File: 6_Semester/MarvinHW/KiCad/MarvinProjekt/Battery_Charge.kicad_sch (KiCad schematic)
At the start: 13 parts, among them U5 DW01A, U6 FS8205A, U7 HM4056H

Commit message: add comonents to BoM
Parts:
- BT1: OrderNow (none) -> x; digikey (none) -> 36-1043P-ND
- U5: LCSC Part (none) -> C351410; OrderNow (none) -> x
- U6: LCSC Part (none) -> C7499846; OrderNow (none) -> x
- U7: OrderNow (none) -> x
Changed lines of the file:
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@@
+			)
+		)
+		(property "OrderNow" ""
+			(at 156.21 95.25 0)
+			(effects
+				(font
+					(size 1.27 1.27)
+				)
+				(hide yes)
 			)
 		)
@@
 			)
 		)
+		(property "OrderNow" ""
+			(at 105.41 92.71 0)
+			(effects
+				(font
+					(size 1.27 1.27)
+				)
+				(hide yes)
+			)
+		)
 		(pin "2"
 		)
@@
 			)
 		)
+		(property "OrderNow" ""
+			(at 105.41 82.55 0)
+			(effects
+				(font
+					(size 1.27 1.27)
+				)
+				(hide yes)
+			)
+		)
 		(pin "1"
 		)
@@
 		)
 		(property "Description" "Resistor"
+			(at 191.77 106.68 0)
+			(effects
+				(font
+					(size 1.27 1.27)
+				)
+				(hide yes)
+			)
+		)
+		(property "OrderNow" ""
 			(at 191.77 106.68 0)
 			(effects
@@
 			)
 		)
+		(property "OrderNow" "x"
+			(at 119.38 92.71 0)
+			(effects
+				(font
+					(size 1.27 1.27)
+				)
+				(hide yes)
+			)
+		)
+		(property "LCSC Part" "C351410"
+			(at 119.38 92.71 0)
+			(effects
+				(font
+					(size 1.27 1.27)
+				)
+				(hide yes)
+			)
+		)
 		(pin "6"
 		)
@@
 			)
 		)
+		(property "OrderNow" "x"
+			(at 179.07 96.52 0)
+			(effects
+				(font
+					(size 1.27 1.27)
+				)
+				(hide yes)
+			)
+		)
 		(pin "3"
 		)
@@
 		)
 		(property "Description" "Unpolarized capacitor"
+			(at 143.51 99.06 0)
+			(effects
+				(font
+					(size 1.27 1.27)
+				)
+				(hide yes)
+			)
+		)
+		(property "OrderNow" ""
 			(at 143.51 99.06 0)
 			(effects
@@
 			)
 		)
+		(property "OrderNow" ""
+			(at 135.89 95.25 0)
+			(effects
+				(font
+					(size 1.27 1.27)
+				)
+				(hide yes)
+			)
+		)
 		(pin "1"
 		)
@@
 			)
 		)
+		(property "OrderNow" ""
+			(at 162.56 99.06 0)
+			(effects
+				(font
+					(size 1.27 1.27)
+				)
+				(hide yes)
+			)
+		)
 		(pin "1"
 		)
@@
 			)
 		)
+		(property "OrderNow" ""
+			(at 156.21 102.87 0)
+			(effects
+				(font
+					(size 1.27 1.27)
+				)
+				(hide yes)
+			)
+		)
 		(pin "1"
 		)
@@
 			)
 		)
+		(property "OrderNow" "x"
+			(at 97.79 88.9 0)
+			(effects
+				(font
+					(size 1.27 1.27)
+				)
+				(hide yes)
+			)
+		)
+		(property "digikey" "36-1043P-ND"
+			(at 97.79 88.9 0)
+			(effects
+				(font
+					(size 1.27 1.27)
+				)
+				(hide yes)
+			)
+		)
 		(pin "1"
 		)
@@
 			)
 		)
+		(property "OrderNow" "x"
+			(at 119.38 109.22 0)
+			(effects
+				(font
+					(size 1.27 1.27)
+				)
+				(hide yes)
+			)
+		)
+		(property "LCSC Part" "C7499846"
+			(at 119.38 109.22 0)
+			(effects
+				(font
+					(size 1.27 1.27)
+				)
+				(hide yes)
+			)
+		)
 		(pin "1"
 		)
@@
 			(at 149.86 95.25 0)
 			(effects
+				(font
+					(size 1.27 1.27)
+				)
+				(hide yes)
+			)
+		)
+		(property "OrderNow" ""
+			(at 149.86 95.25 0)
+			(effects

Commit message: finish evaluat components
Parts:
- R34: now not fitted
- U7: LCSC Part (none) -> C16581
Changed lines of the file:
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@@
 		(in_bom yes)
 		(on_board yes)
-		(dnp no)
+		(dnp yes)
 		(property "Reference" "R34"
 			(at 103.378 85.344 90)
@@
 			(at 179.07 96.52 0)
 			(effects
+				(font
+					(size 1.27 1.27)
+				)
+				(hide yes)
+			)
+		)
+		(property "LCSC Part" "C16581"
+			(at 179.07 96.52 0)
+			(effects

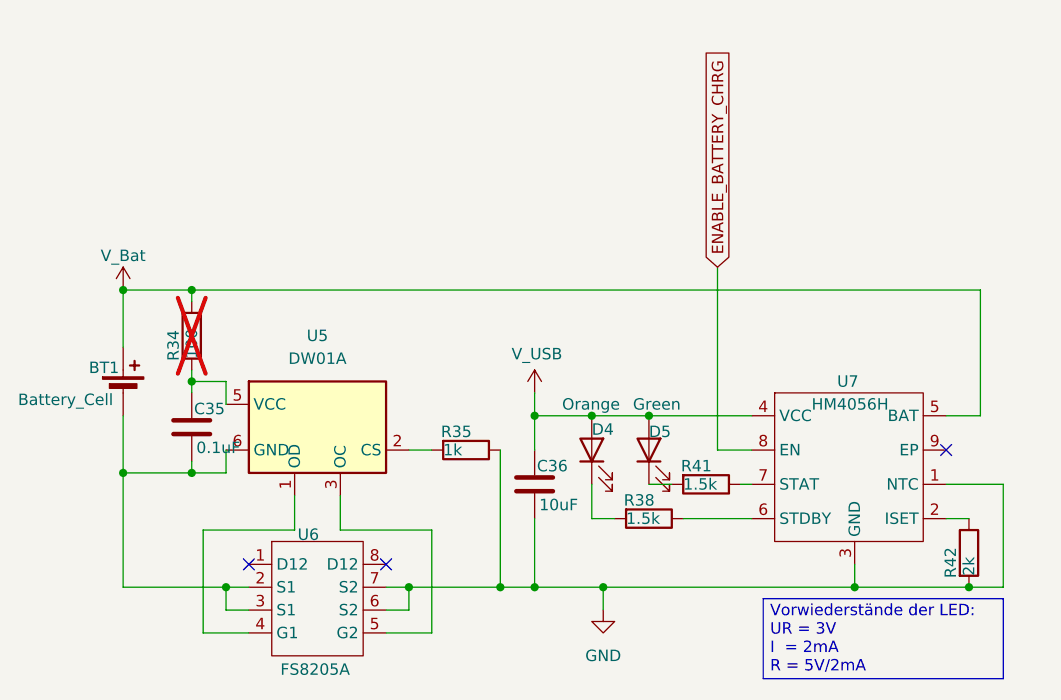
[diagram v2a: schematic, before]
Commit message: change dnp from yes to no
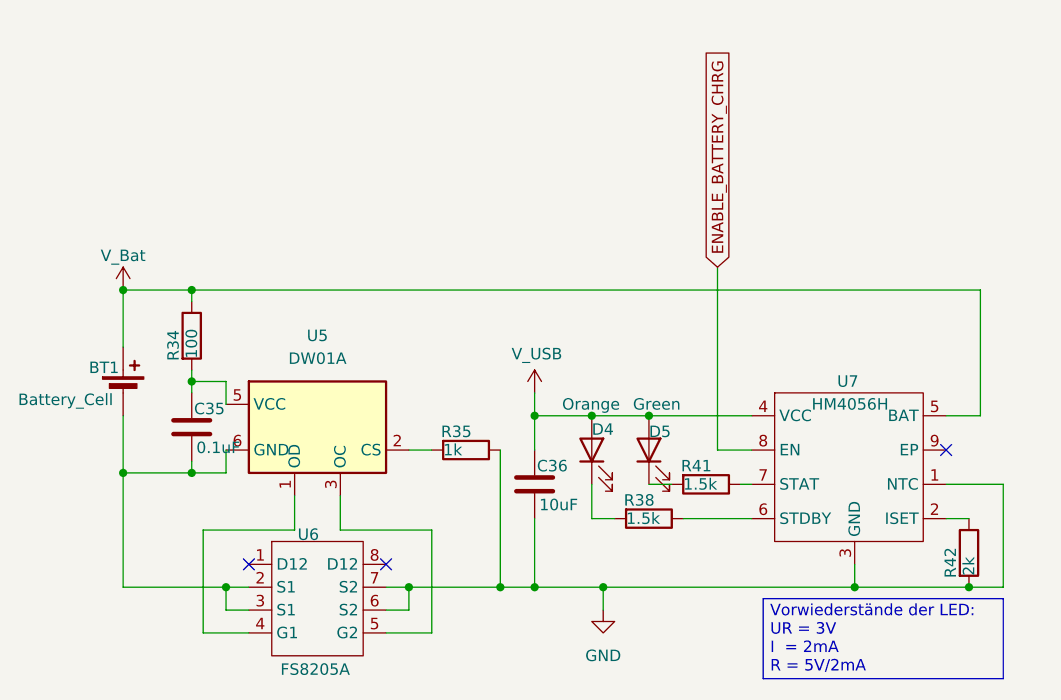
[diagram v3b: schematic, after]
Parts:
- R34: now fitted
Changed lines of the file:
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@@
 		(in_bom yes)
 		(on_board yes)
-		(dnp yes)
+		(dnp no)
 		(property "Reference" "R34"
 			(at 103.378 85.344 90)
